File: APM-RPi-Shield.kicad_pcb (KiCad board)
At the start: 2 copper layers, 37.2 x 56.2 mm, 31 parts, among them IC1 ADS1115, IC2 PCA9685, P1 CONN_13X2, P2 BMP180, P3 ADC, P4 SPI, P5 MPU9250, P6 I2C, P7 UART, P8 CONN_03X16

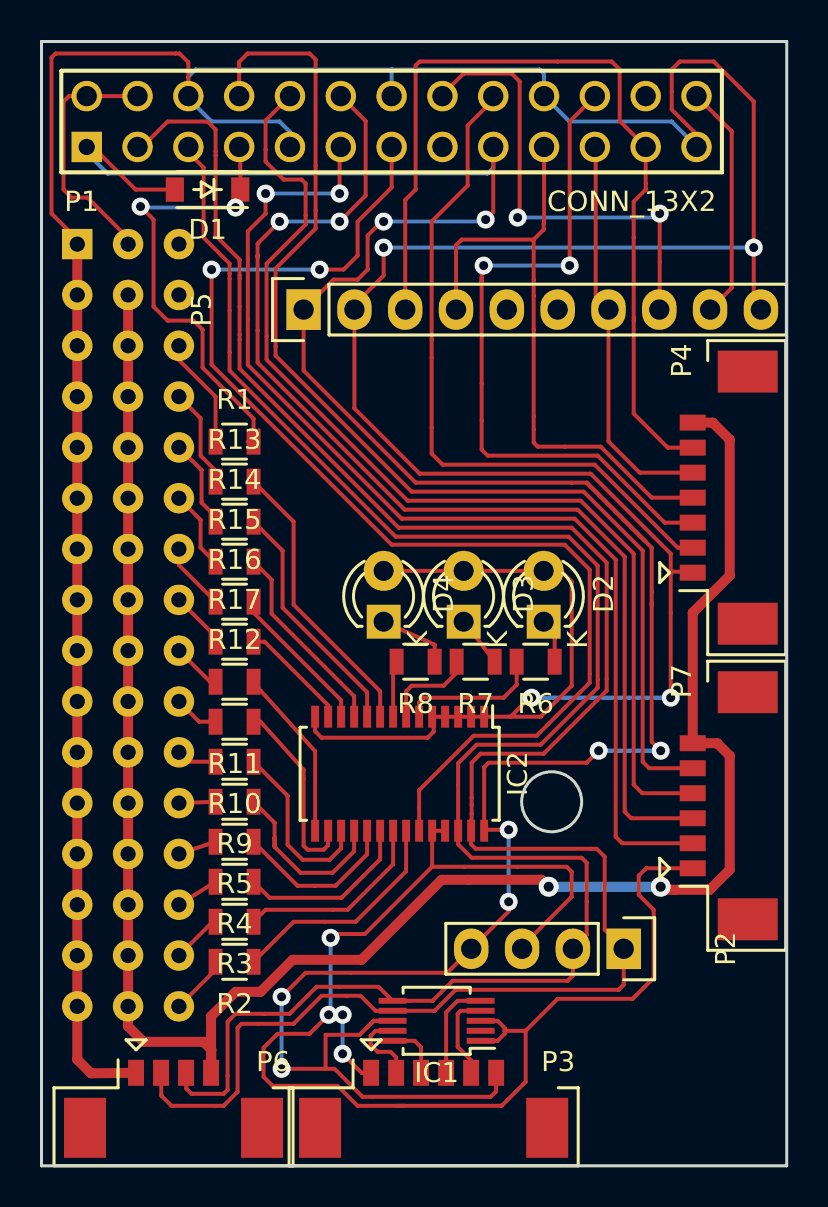
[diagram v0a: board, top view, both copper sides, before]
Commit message: Change for 0.3mm row two-side
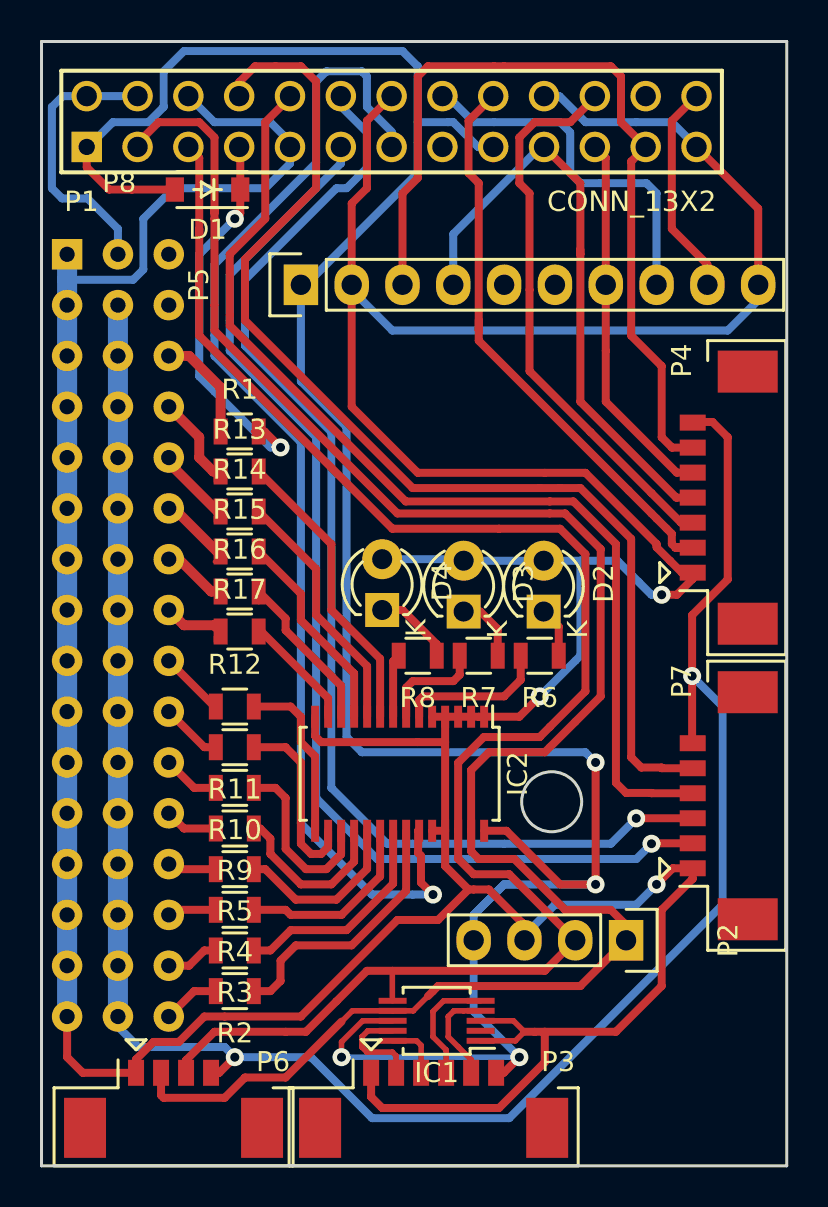
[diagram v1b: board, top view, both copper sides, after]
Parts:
- moved R2 1.47 mm to (153.2, 172.5)
- moved R3 1.43 mm to (153.2, 170.4)
- moved R4 1.40 mm to (153.2, 168.4)
- moved R5 1.37 mm to (153.2, 166.4)
- moved R9 1.34 mm to (153.2, 164.3)
- moved R10 1.31 mm to (153.2, 162.3)
- moved R11 1.27 mm to (153.2, 160.3)
- moved P5 1.25 mm to (156.5, 137.2)
- moved R12 1.24 mm to (153.2, 158.2)
- moved P8 0.72 mm to (144.8, 135.6)
- moved D4 0.59 mm to (160.5, 153.4)
- moved R1 0.57 mm to (153.4, 144.5)
- moved R13 0.57 mm to (153.4, 146.5)
- moved R14 0.57 mm to (153.4, 148.5)
- moved R15 0.57 mm to (153.4, 150.5)
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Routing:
- net GND: track 287.4 -> 264.8 mm, vias 8 -> 3
- net +3V3: track 137.8 -> 127.8 mm, vias 8 -> 4
- net /GPIO25: track 35.7 -> 28.2 mm, vias 2 -> 0
- net /GPIO1(SCL): track 91.9 -> 85.7 mm
- net /GPIO0(SDA): track 102.8 -> 97.3 mm
- net /GPIO23: track 24.0 -> 18.6 mm, vias 2 -> 0
- net /BEC_5V: track 100.5 -> 104.3 mm
- net /GPIO24: track 35.2 -> 31.7 mm
- net /GPIO4(PPM): track 23.3 -> 19.8 mm
- net /GPIO18: track 56.9 -> 60.1 mm, vias 2 -> 1
- net /GPIO11(SCLK): track 46.2 -> 43.5 mm
- net Net-(IC2-Pad22): track 11.6 -> 13.4 mm
- net Net-(P8-Pad35): track 6.90 -> 5.45 mm
- net +5V: track 12.7 -> 14.0 mm
- net Net-(IC1-Pad4): track 4.50 -> 5.68 mm
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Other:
- net class Default: trace_width 0.2 -> 0.4
- net class Power: clearance 0.2 -> 0.5; trace_width 0.5 -> 1
- net class mini added: clearance 0.2, trace_width 0.28, via_dia 0.9, via_drill 0.6

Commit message: Add pdf result. Small fixes
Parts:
- moved R1 112.1 mm to (65.7, 74.7), turned to 270 degrees
- moved D1 109.8 mm to (65.3, 64.7)
- moved P4 109.8 mm to (92.3, 80.1)
- moved P7 109.8 mm to (92.3, 95.5)
- moved R7 109.8 mm to (78.9, 88.0)
- moved R8 109.8 mm to (75.8, 88.0)
- moved D2 109.8 mm to (82.1, 85.8)
- moved D3 109.8 mm to (78.1, 85.8)
- moved IC1 109.8 mm to (76.8, 106.2)
- moved IC2 109.8 mm to (74.9, 93.9)
- moved P1 109.8 mm to (74.5, 61.3)
- moved P2 109.8 mm to (86.2, 102.2)
- moved P3 109.8 mm to (76.6, 111.6)
- moved P5 109.8 mm to (70.0, 69.5)
- moved P6 109.8 mm to (63.6, 111.6)
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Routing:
- net /BEC_5V: track 104.3 -> 109.7 mm
- net +3V3: track 127.8 -> 131.6 mm
- net Net-(P8-Pad35): track 5.45 -> 2.59 mm
- net /RXD: track 52.5 -> 50.0 mm
- net GND: track 264.8 -> 267.2 mm
- net /TXD: track 57.0 -> 54.8 mm
- net /GPIO0(SDA): track 97.3 -> 95.9 mm
- net /GPIO24: track 31.7 -> 30.4 mm
- net /GPIO4(PPM): track 19.8 -> 21.1 mm, vias 2 -> 1
- net /GPIO18: track 60.1 -> 61.1 mm
- net /GPIO25: track 28.2 -> 28.9 mm
- net /GPIO1(SCL): track 85.7 -> 85.0 mm
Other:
- outline, holes or cut-outs redrawn
- net class Default: via_dia 0.9 -> 1.6; via_drill 0.6 -> 0.9
- board text added: "37 mm"
- board text added: "56 mm"

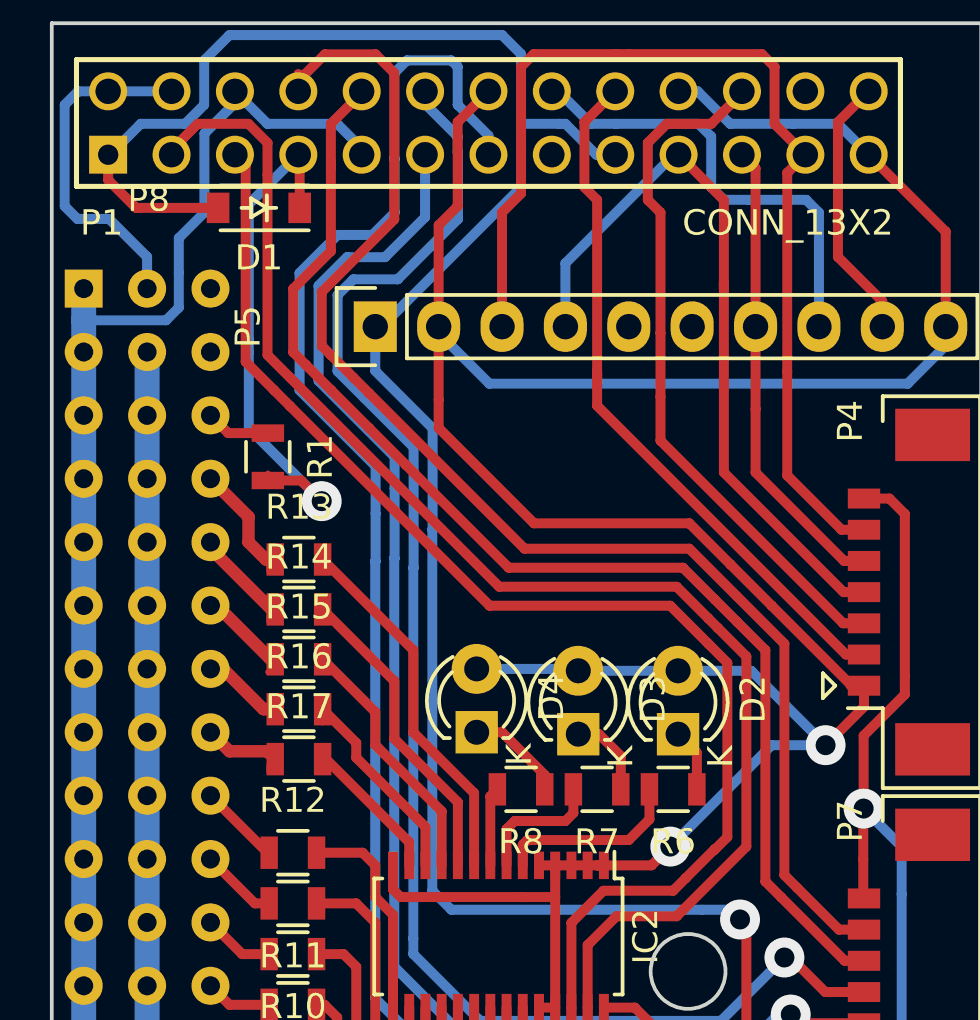
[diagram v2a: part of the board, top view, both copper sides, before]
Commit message: fix on practic use
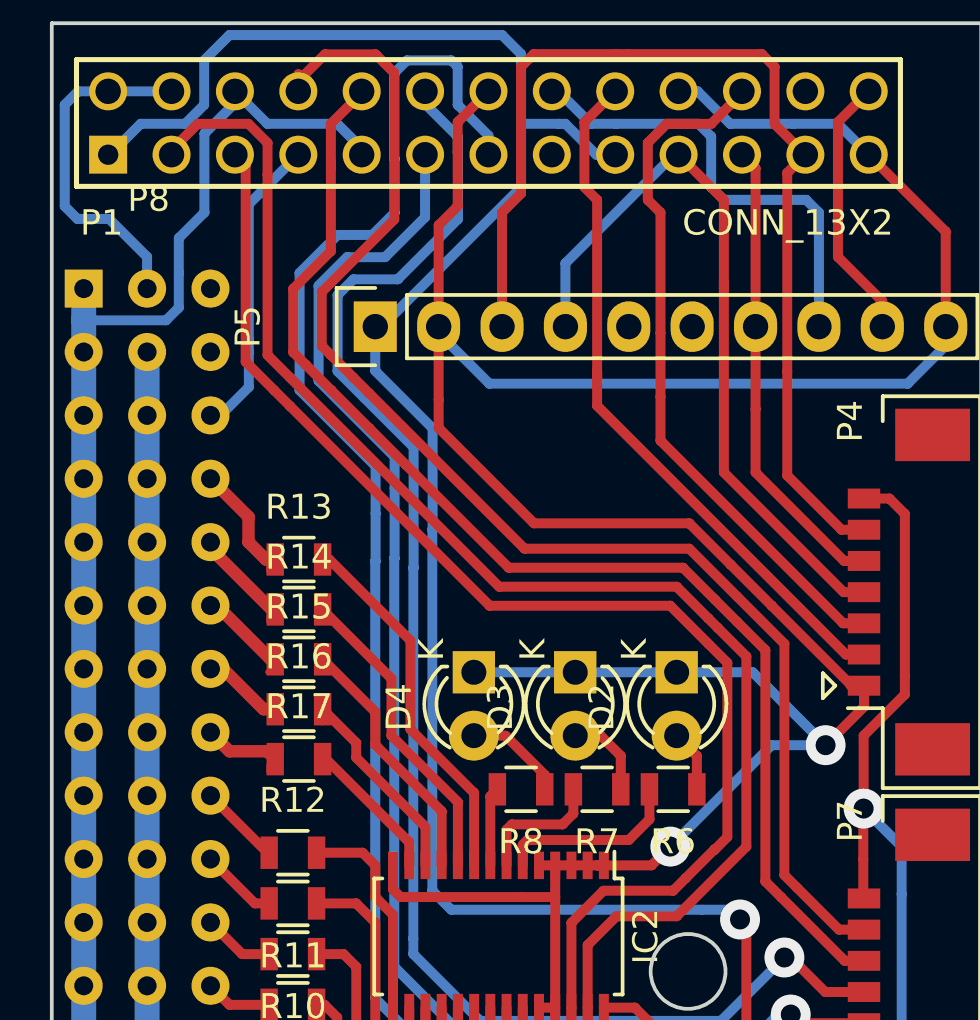
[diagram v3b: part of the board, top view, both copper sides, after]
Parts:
- removed D1: 1N4148, Diodes_SMD:SOD-123
- removed R1: 1K, Resistors_SMD:R_0805
- moved D3 2.48 mm to (78.0, 83.3), turned to 270 degrees
- moved D2 2.48 mm to (82.0, 83.3), turned to 270 degrees
- moved D4 2.41 mm to (73.9, 83.3), turned to 270 degrees
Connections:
- D2 pad 1: Net-(D2-Pad1) -> GND
- D2 pad 2: GND -> Net-(D2-Pad2)
- D3 pad 1: Net-(D3-Pad1) -> GND
- D3 pad 2: GND -> Net-(D3-Pad2)
- D4 pad 1: Net-(D4-Pad1) -> GND
- D4 pad 2: GND -> Net-(D4-Pad2)
- P8 pad 35: Net-(P8-Pad35) -> /GPIO4(PPM)
- R6 pad 1: Net-(D2-Pad1) -> Net-(D2-Pad2)
- R7 pad 1: Net-(D3-Pad1) -> Net-(D3-Pad2)
- R8 pad 1: Net-(D4-Pad1) -> Net-(D4-Pad2)
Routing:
- net /GPIO4(PPM): track 21.1 -> 12.2 mm, vias 1 -> 0
- net +3V3: track 131.6 -> 125.3 mm
- net Net-(D3-Pad2): track 0.00 -> 5.21 mm
- net Net-(D4-Pad2): track 0.00 -> 4.07 mm
- net Net-(D4-Pad1): track 4.01 -> 0.00 mm
- net Net-(D3-Pad1): track 3.61 -> 0.00 mm
- net Net-(P8-Pad35): track 2.59 -> 0.00 mm
- net Net-(D2-Pad1): track 2.52 -> 0.00 mm
- net Net-(D2-Pad2): track 0.00 -> 2.49 mm
- net GND: track 267.2 -> 265.5 mm
- net Net-(IC2-Pad7): track 5.90 -> 5.35 mm
